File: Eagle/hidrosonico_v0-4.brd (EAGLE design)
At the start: 68.6 x 53.3 mm, 7 parts, among them J1 RJ11, U1 ARDUINOR3-DIMENSION

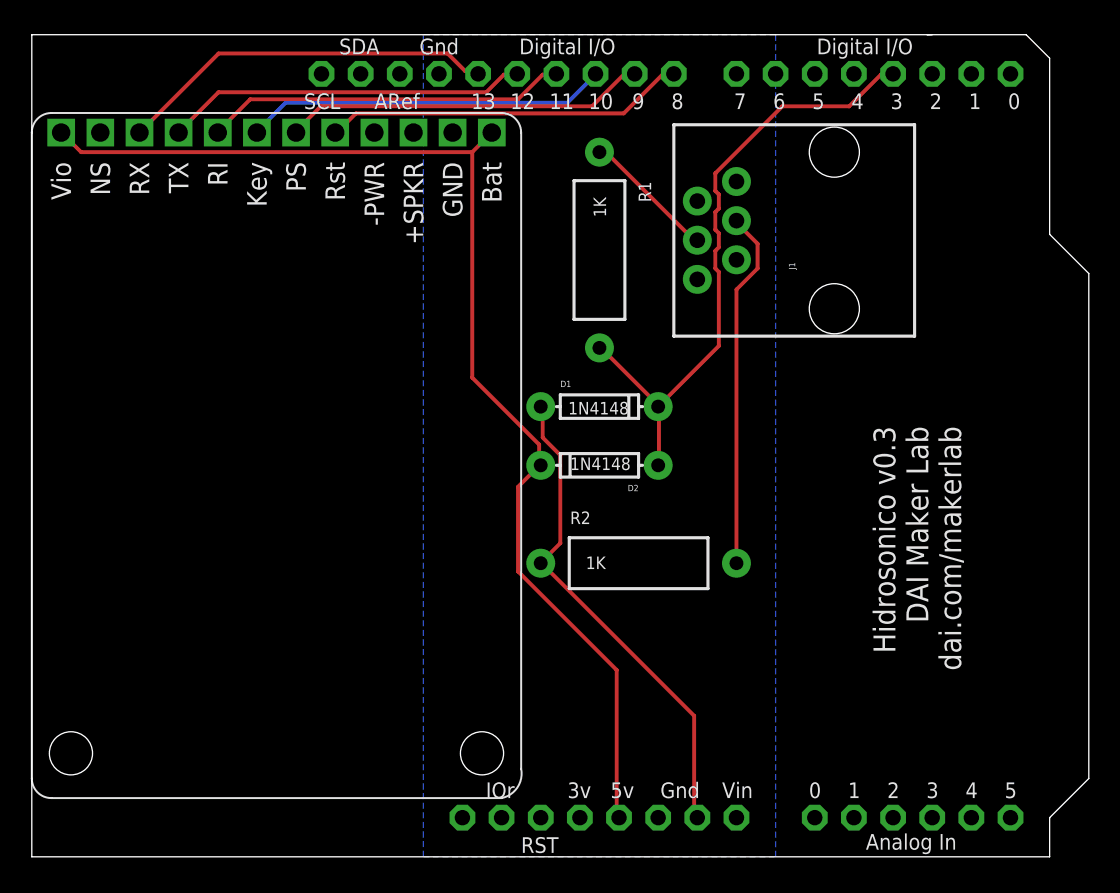
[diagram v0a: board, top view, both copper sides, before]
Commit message: Updated Eagle board file
Improved PCB design includes easier access to SIM slot on FONA and
battery and solar jacks on Stalker.
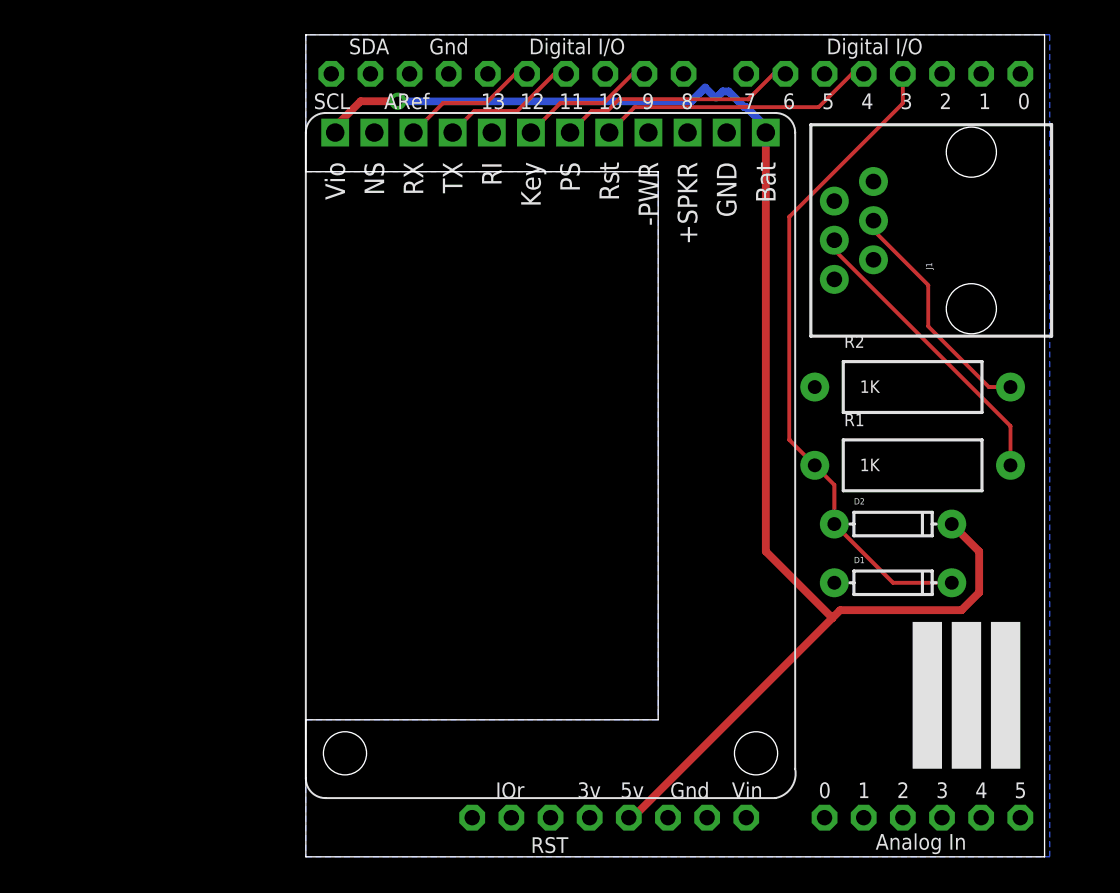
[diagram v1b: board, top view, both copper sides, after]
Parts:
- removed U1: ARDUINOR3-DIMENSION, adafruit:ARDUINOR3
- added U2: ARDUINOR3-DIMENSION, dai-maker-lab:ARDUINOR3
- D1, D2: value 1N4148 -> (none)
- U$1: value ADAFRUIT_FONA -> ADAFRUIT_FONA800
- moved R1 24.7 mm to (57.1, 25.4), turned to 0 degrees
- moved D1 22.2 mm to (55.9, 17.8)
- moved R2 21.1 mm to (57.1, 30.5)
- moved D2 19.4 mm to (55.9, 21.6), turned to 0 degrees
- moved U$1 17.8 mm to (49.5, 48.3)
- moved J1 8.89 mm to (61.0, 40.6)
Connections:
- removed net GND2: U1.GND2
- removed net KEY: U$1.KEY, U1.D10
- removed net N$10 (its old number): D1.C, D2.A, R1.P$2, U1.D3
- removed net PWR: D2.C, U$1.BAT, U$1.VIO, U1.5V
- removed net RI: U$1.RI, U1.D11
- removed net RST: U$1.RST, U1.D8
- removed net RX: U$1.RX, U1.D13
- removed net TX: U$1.TX, U1.D12
- new net GND1: U2.GND1
- new net N$1: U$1.RST, U2.D4
- new net N$3: U$1.KEY, U2.D9
- new net N$4: U$1.TX, U2.D11
- new net N$5: U$1.RX, U2.D12
- new net VCC+: D2.C, U$1.BAT, U$1.VIO, U2.5V
- net 3V: now also U2.3V; no longer U1.3V
- net GND: now also D1.A, R2.P$1, U2.GND, U2.GND2; no longer U1.GND
- net N$2: now also U2.D6; no longer U1.D9
- net N$8: now also R1.P$2; no longer R1.P$1
- net N$9: now also D1.C, D2.A, R1.P$1, U2.D3; no longer D1.A, R2.P$1, U1.GND1
- net VIN: now also U2.VIN; no longer U1.VIN
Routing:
- net VCC+: track 0.00 -> 98.4 mm, vias 0 -> 1
- net PWR: track 77.3 -> 0.00 mm
- net N$10 (its old number): track 40.7 -> 0.00 mm
- net RX: track 24.7 -> 0.00 mm
- net KEY: track 23.6 -> 0.00 mm
- net RI: track 23.6 -> 0.00 mm
- net TX: track 23.5 -> 0.00 mm
- net RST: track 23.5 -> 0.00 mm
- net N$1: track 0.00 -> 18.1 mm
- net N$9: track 31.9 -> 42.7 mm
- net N$8: track 8.72 -> 19.3 mm
- net N$3: track 0.00 -> 8.94 mm
- net N$5: track 0.00 -> 8.94 mm
- net N$4: track 0.00 -> 8.94 mm
- net N$2: track 23.6 -> 15.5 mm
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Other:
- board size 68.6 x 53.3 mm -> 47.9 x 53.3 mm
- board text added: "DAI Maker Lab http://dai.com/makerlab"
- board text added: "Hidrosónico v0.4"
- board text removed: "Hidrosonico v0.3 DAI Maker Lab dai.com/makerlab"
